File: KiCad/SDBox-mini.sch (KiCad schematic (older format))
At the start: 26 parts, among them J1 DB25_Male, J2 Conn_02x03_Odd_Even, J3 Micro_SD_Card, J4 USB_B_Micro, U1 LM1117-3.3, U2 ATmega328P-AU, U3 74LVC3G17, U4 74HCT2G17, Y1 Crystal_GND24_Small

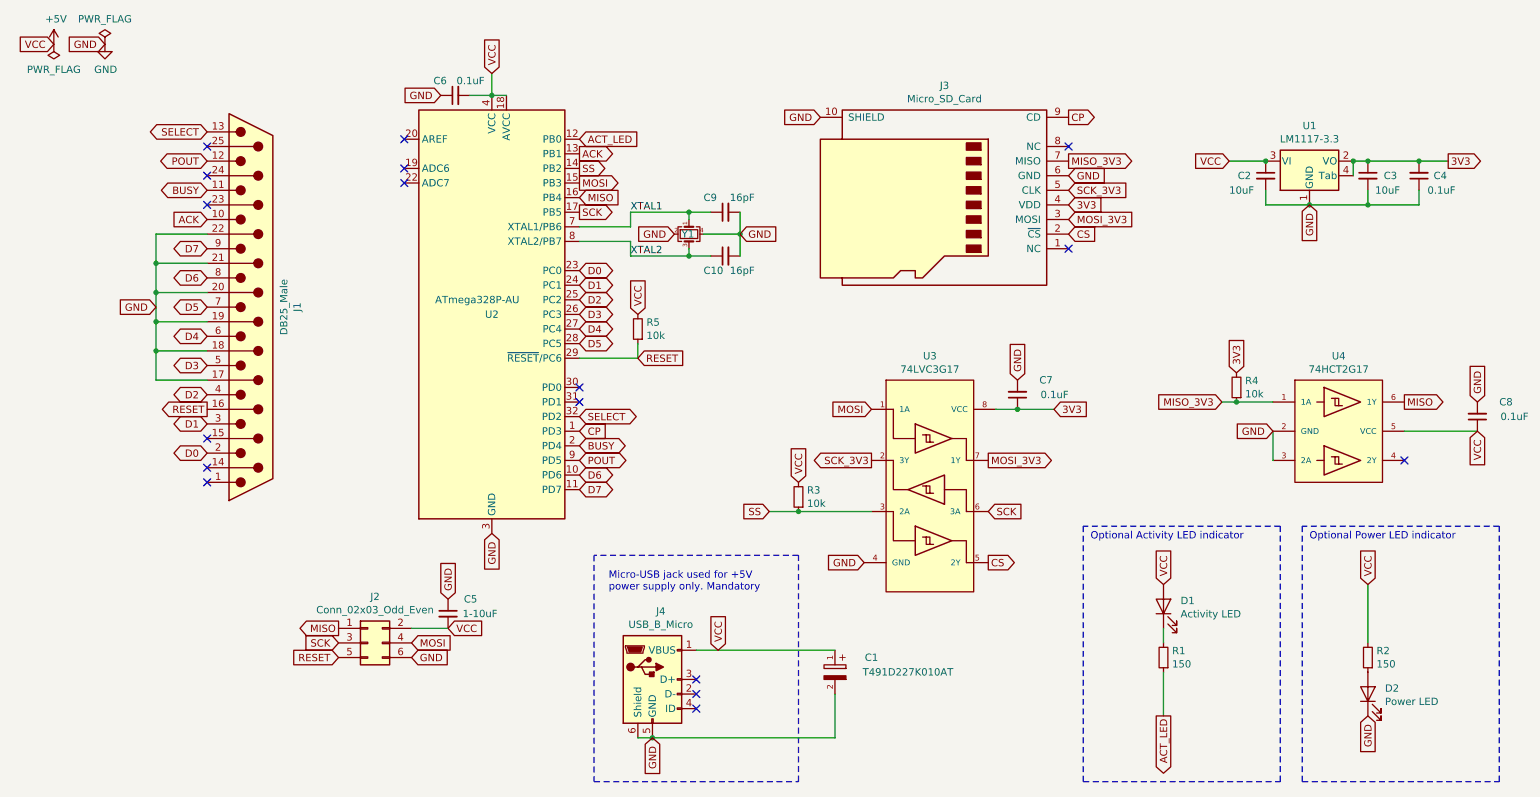
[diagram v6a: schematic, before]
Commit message: Removed capacitor at VCC-pin ICSP-header and renumbered Caps
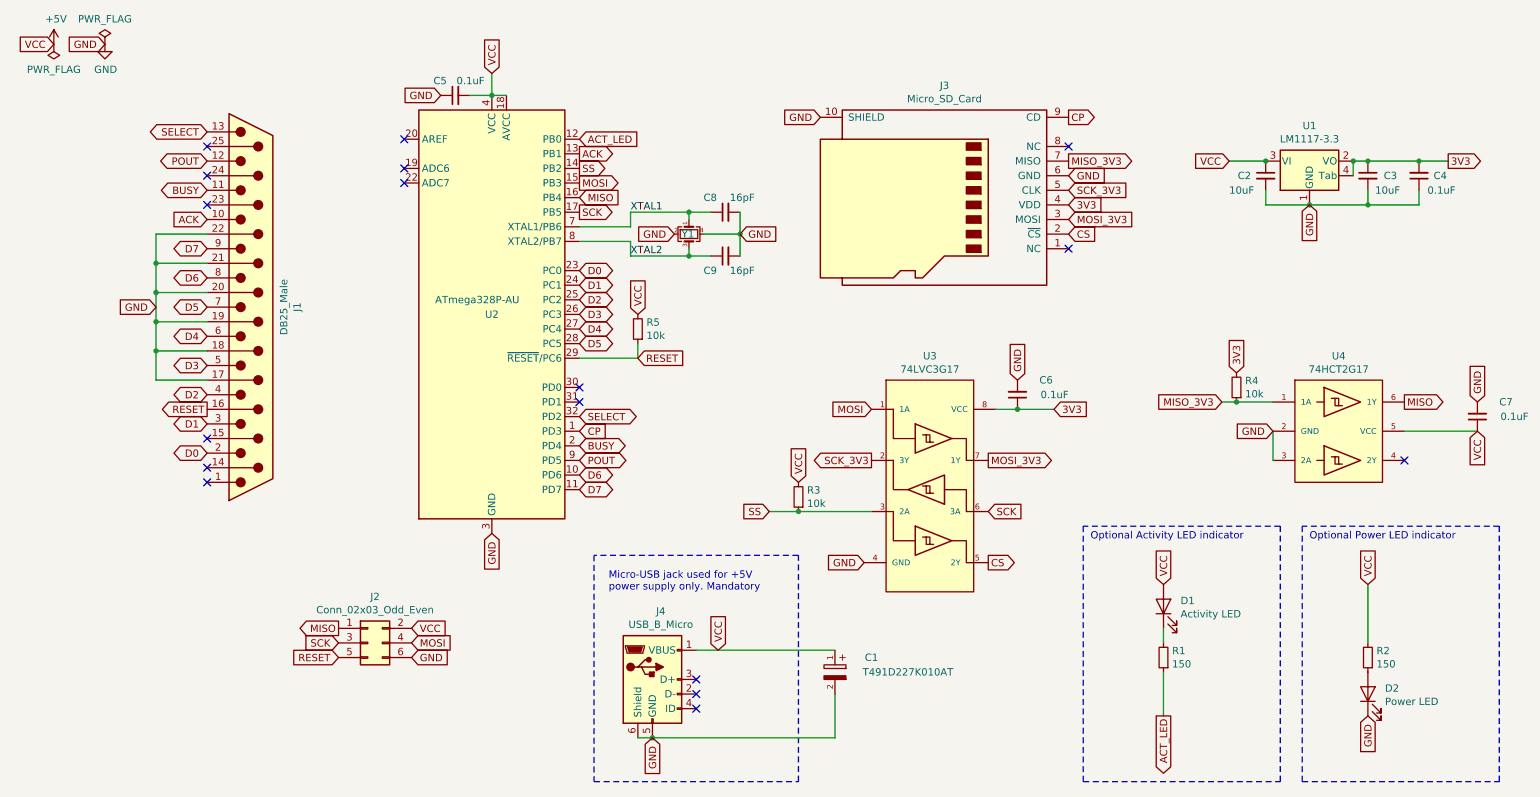
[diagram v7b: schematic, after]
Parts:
- removed C5: 1-10uF, Capacitor_SMD:C_0805_2012Metric_Pad1.15x1.40mm_HandSolder, symbol Device:C_Small
- renumbered C6 to C5, C7 to C6, C8 to C7, C9 to C8, C10 to C9
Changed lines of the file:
@@
 GND
 $Comp
-L Device:C_Small C9
+L Device:C_Small C8
 U 1 1 60FA06FB
 P 5550 2100
-F 0 "C9" V 5650 2250 50  0000 R CNN
+F 0 "C8" V 5650 2250 50  0000 R CNN
 F 1 "16pF" V 5650 1900 50  0000 L CNN
 F 2 "Capacitor_SMD:C_0603_1608Metric_Pad1.05x0.95mm_HandSolder" H 5550 2100 50  0001 C CNN
@@
 	4900 2100 5300 2100
 $Comp
-L Device:C_Small C10
+L Device:C_Small C9
 U 1 1 60FA5116
 P 5550 2400
-F 0 "C10" V 5450 2550 50  0000 R CNN
+F 0 "C9" V 5450 2550 50  0000 R CNN
 F 1 "16pF" V 5450 2200 50  0000 L CNN
 F 2 "Capacitor_SMD:C_0603_1608Metric_Pad1.05x0.95mm_HandSolder" H 5550 2400 50  0001 C CNN
@@
 Connection ~ 5650 2250
 $Comp
-L Device:C_Small C6
+L Device:C_Small C5
 U 1 1 60FA7C64
 P 3700 1300
-F 0 "C6" V 3800 1450 50  0000 R CNN
+F 0 "C5" V 3800 1450 50  0000 R CNN
 F 1 "0.1uF" V 3800 1100 50  0000 L CNN
 F 2 "Capacitor_SMD:C_0603_1608Metric_Pad1.05x0.95mm_HandSolder" H 3700 1300 50  0001 C CNN
@@
 Text GLabel 10500 1750 2    50   Output ~ 0
 3V3
-Text GLabel 3650 4950 2    50   Input ~ 0
+Text GLabel 3400 4950 2    50   Input ~ 0
 VCC
 Text GLabel 3400 5150 2    50   Input ~ 0
 GND
 $Comp
-L Device:C_Small C7
+L Device:C_Small C6
 U 1 1 61017825
 P 7550 3350
-F 0 "C7" H 7400 3250 50  0000 R CNN
+F 0 "C6" H 7400 3250 50  0000 R CNN
 F 1 "0.1uF" H 7200 3350 50  0000 L CNN
 F 2 "Capacitor_SMD:C_0603_1608Metric_Pad1.05x0.95mm_HandSolder" H 7550 3350 50  0001 C CNN
@@
 $EndComp
 $Comp
-L Device:C_Small C8
+L Device:C_Small C7
 U 1 1 61087309
 P 10700 3500
-F 0 "C8" H 10550 3400 50  0000 R CNN
+F 0 "C7" H 10550 3400 50  0000 R CNN
 F 1 "0.1uF" H 10350 3500 50  0000 L CNN
 F 2 "Capacitor_SMD:C_0603_1608Metric_Pad1.05x0.95mm_HandSolder" H 10700 3500 50  0001 C CNN
@@
 Wire Wire Line
 	8550 5250 8550 5550
-$Comp
-L Device:C_Small C5
-U 1 1 61173877
-P 3650 4850
-F 0 "C5" H 3850 4950 50  0000 R CNN
-F 1 "1-10uF" H 3750 4850 50  0000 L CNN
-F 2 "Capacitor_SMD:C_0805_2012Metric_Pad1.15x1.40mm_HandSolder" H 3650 4850 50  0001 C CNN
-F 3 "~" H 3650 4850 50  0001 C CNN
-	1    3650 4850
-	1    0    0    -1
-$EndComp
-Wire Wire Line
-	3650 4950 3400 4950
-Text GLabel 3650 4750 1    50   Input ~ 0
-GND
 NoConn ~ 3350 1600
 Text GLabel 4550 1600 2    50   Input ~ 0

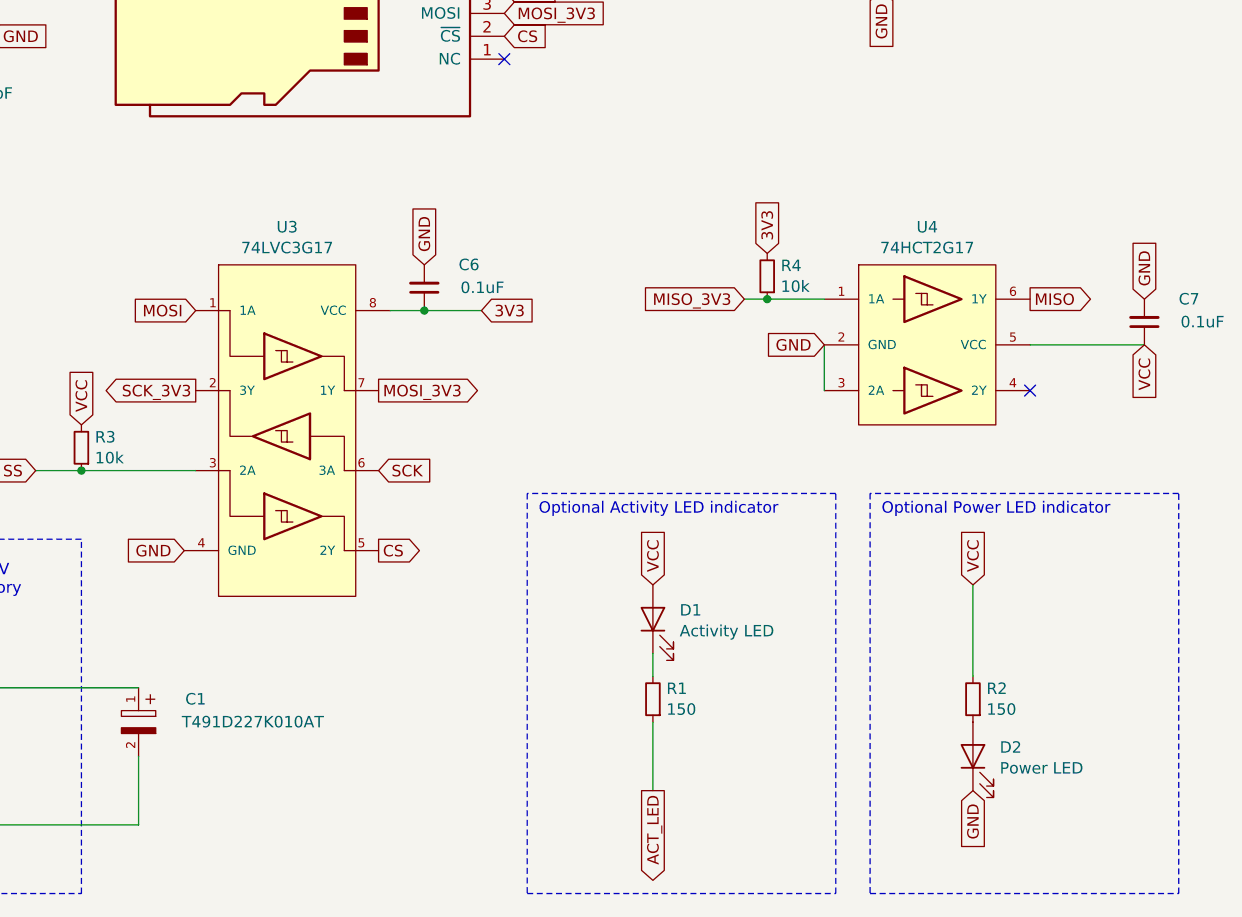
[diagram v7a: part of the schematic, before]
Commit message: Changed U4 to a 74LVC1G17 and made SOT-353_SC-70-5_Custom_Handsoldering footprint
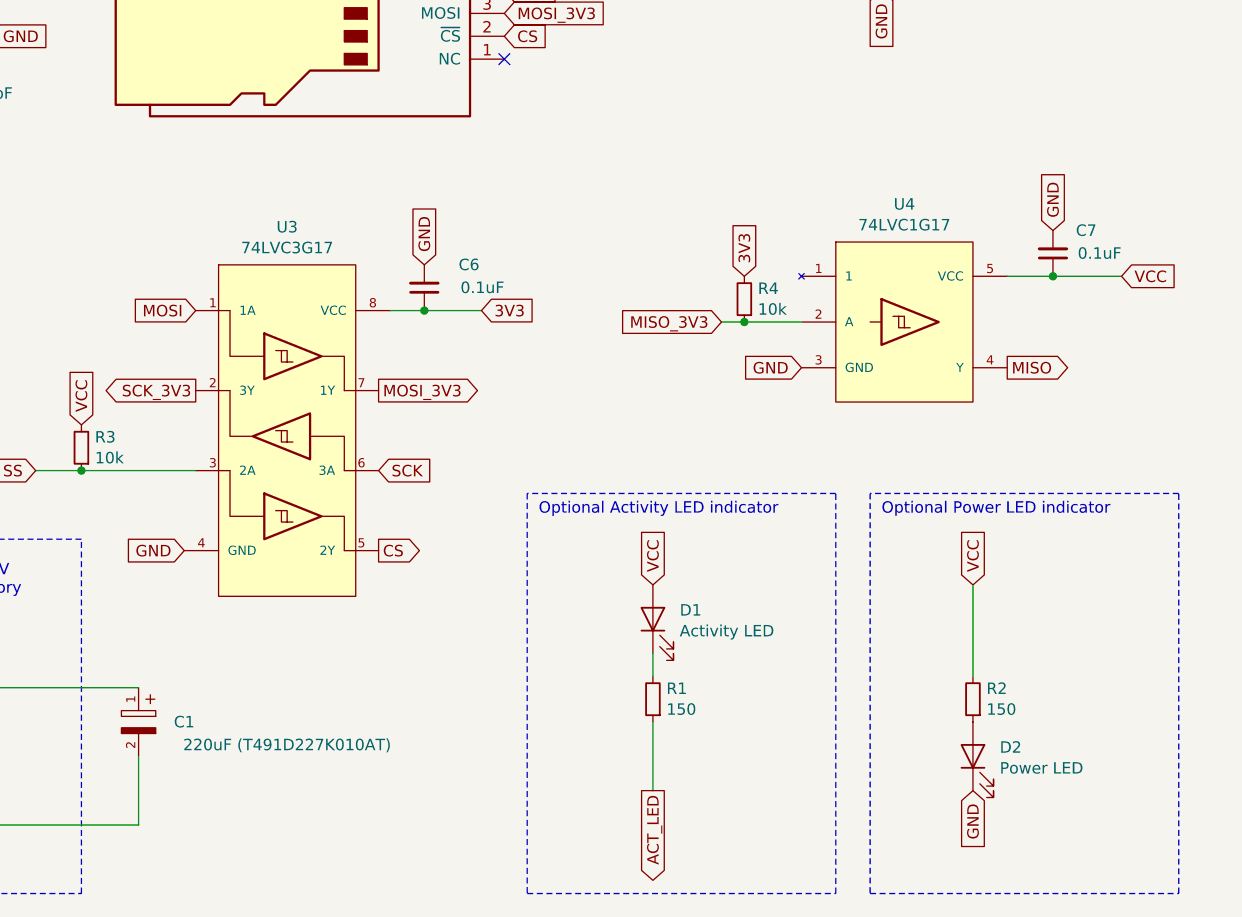
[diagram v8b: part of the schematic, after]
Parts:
- removed U4: 74HCT2G17, Package_SO:TSOP-6_1.65x3.05mm_P0.95mm, symbol SDBox-mini:74HCT2G17
- added U4: 74LVC1G17, SDBox-mini:SOT-353_SC-70-5_Custom_Handsoldering, symbol SDBox-mini:74LVC1G17
- C1: value T491D227K010AT -> 220uF (T491D227K010AT)
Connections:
- net +5V: now also U4.5 (VCC)
- net GND: now also U4.3 (GND)
- net MISO: now also U4.4 (Y)
- net MISO_3V3: now also U4.2 (A)
- no-connect marks 17 -> 16
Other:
- moved on the sheet: C7, R4
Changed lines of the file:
@@
 RESET
 NoConn ~ 7900 2350
-Text GLabel 10200 3400 2    50   Output ~ 0
+Text GLabel 10100 3700 2    50   Output ~ 0
 MISO
 Text GLabel 7900 1850 2    50   Input ~ 0
@@
 L Device:R_Small R4
 U 1 1 6101E2BD
-P 9050 3300
-F 0 "R4" H 8991 3254 50  0000 R CNN
-F 1 "10k" H 8991 3345 50  0000 R CNN
-F 2 "Resistor_SMD:R_0603_1608Metric_Pad1.05x0.95mm_HandSolder" H 9050 3300 50  0001 C CNN
-F 3 "~" H 9050 3300 50  0001 C CNN
-	1    9050 3300
-	-1   0    0    1
-$EndComp
-Text GLabel 9050 3200 1    50   Input ~ 0
+P 8950 3400
+F 0 "R4" H 8891 3354 50  0000 R CNN
+F 1 "10k" H 8891 3445 50  0000 R CNN
+F 2 "Resistor_SMD:R_0603_1608Metric_Pad1.05x0.95mm_HandSolder" H 8950 3400 50  0001 C CNN
+F 3 "~" H 8950 3400 50  0001 C CNN
+	1    8950 3400
+	-1   0    0    1
+$EndComp
+Text GLabel 8950 3300 1    50   Input ~ 0
 3V3
 Text GLabel 7900 2150 2    50   Input ~ 0
@@
 Text GLabel 7900 1750 2    50   Output ~ 0
 MISO_3V3
-Text GLabel 8950 3400 0    50   Input ~ 0
+Text GLabel 8850 3500 0    50   Input ~ 0
 MISO_3V3
 Wire Wire Line
-	8950 3400 9050 3400
+	8850 3500 8950 3500
 Text GLabel 6550 3800 0    50   Output ~ 0
 SCK_3V3
@@
 	7550 3450 7400 3450
 $Comp
-L SDBox-mini:74HCT2G17 U4
-U 1 1 6107F418
-P 9750 3600
-F 0 "U4" H 9750 4115 50  0000 C CNN
-F 1 "74HCT2G17" H 9750 4024 50  0000 C CNN
-F 2 "Package_SO:TSOP-6_1.65x3.05mm_P0.95mm" H 10250 4550 50  0001 C CNN
-F 3 "https://assets.nexperia.com/documents/data-sheet/74HC_HCT2G17.pdf" H 10250 4550 50  0001 C CNN
-	1    9750 3600
-	1    0    0    -1
-$EndComp
-$Comp
 L Device:C_Small C7
 U 1 1 61087309
-P 10700 3500
-F 0 "C7" H 10550 3400 50  0000 R CNN
-F 1 "0.1uF" H 10350 3500 50  0000 L CNN
-F 2 "Capacitor_SMD:C_0603_1608Metric_Pad1.05x0.95mm_HandSolder" H 10700 3500 50  0001 C CNN
-F 3 "~" H 10700 3500 50  0001 C CNN
-	1    10700 3500
-	-1   0    0    1
-$EndComp
-Text GLabel 10700 3400 1    50   Input ~ 0
-GND
-Wire Wire Line
-	10700 3600 10200 3600
-Text GLabel 10700 3600 3    50   Input ~ 0
-VCC
-Wire Wire Line
-	9050 3400 9300 3400
-Connection ~ 9050 3400
-Text GLabel 9300 3600 0    50   Input ~ 0
+P 10300 3200
+F 0 "C7" H 10200 3100 50  0000 R CNN
+F 1 "0.1uF" H 10000 3200 50  0000 L CNN
+F 2 "Capacitor_SMD:C_0603_1608Metric_Pad1.05x0.95mm_HandSolder" H 10300 3200 50  0001 C CNN
+F 3 "~" H 10300 3200 50  0001 C CNN
+	1    10300 3200
+	-1   0    0    1
+$EndComp
+Text GLabel 10300 3100 1    50   Input ~ 0
+GND
+Wire Wire Line
+	10600 3300 10300 3300
+Text GLabel 10600 3300 2    50   Input ~ 0
+VCC
+Wire Wire Line
+	8950 3500 9200 3500
+Connection ~ 8950 3500
+Text GLabel 9200 3700 0    50   Input ~ 0
 GND
 Wire Wire Line
@@
 U 1 1 60F9E387
 P 6300 5300
-F 0 "C1" V 6450 5050 50  0000 C CNN
-F 1 "T491D227K010AT" V 6350 4800 50  0000 C CNN
+F 0 "C1" V 6350 5100 50  0000 C CNN
+F 1 "220uF  (T491D227K010AT)" V 6250 4650 50  0000 C CNN
 F 2 "SDBox-mini:CAPMP7343X430N" H 6300 5300 50  0001 L BNN
 F 3 "" H 6300 5300 50  0001 L BNN
@@
 Text GLabel 3400 5050 2    50   Input ~ 0
 MOSI
-Wire Wire Line
-	9300 3800 9300 3600
-NoConn ~ 10200 3800
 NoConn ~ 4550 3300
 NoConn ~ 4550 3400
@@
 Wire Wire Line
 	6050 4150 6550 4150
+$Comp
+L SDBox-mini:74LVC1G17 U4
+U 1 1 611C568A
+P 9650 3500
+F 0 "U4" H 9650 4015 50  0000 C CNN
+F 1 "74LVC1G17" H 9650 3924 50  0000 C CNN
+F 2 "SDBox-mini:SOT-353_SC-70-5_Custom_Handsoldering" H 10150 4450 50  0001 C CNN
+F 3 "https://www.ti.com/lit/ds/symlink/sn74lvc1g17-q1.pdf" H 10150 4450 50  0001 C CNN
+	1    9650 3500
+	1    0    0    -1
+$EndComp
+Connection ~ 10300 3300
+Wire Wire Line
+	10300 3300 10100 3300
 $EndSCHEMATC
